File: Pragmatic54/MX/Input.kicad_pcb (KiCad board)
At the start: 2 copper layers, 126.5 x 103.6 mm, 109 parts, among them J1 Conn_02x04_Odd_Even, SW1 SW_Push_45deg, SW10 SW_Push_45deg, SW11 SW_Push_45deg, SW12 SW_Push_45deg, SW13 SW_Push_45deg, SW14 SW_Push_45deg, SW15 SW_Push_45deg, SW16 SW_Push_45deg, SW17 SW_Push_45deg, SW18 SW_Push_45deg, SW19 SW_Push_45deg, SW2 SW_Push_45deg, SW20 SW_Push_45deg, SW21 SW_Push_45deg, SW22 SW_Push_45deg, SW23 SW_Push_45deg, SW24 SW_Push_45deg, SW25 SW_Push_45deg, SW26 SW_Push_45deg, SW27 SW_Push_45deg, SW28 SW_Push_45deg, SW29 SW_Push_45deg, SW3 SW_Push_45deg, SW30 SW_Push_45deg, SW31 SW_Push_45deg, SW32 SW_Push_45deg, SW33 SW_Push_45deg, SW34 SW_Push_45deg, SW35 SW_Push_45deg, SW36 SW_Push_45deg, SW37 SW_Push_45deg, SW38 SW_Push_45deg, SW39 SW_Push_45deg, SW4 SW_Push_45deg, SW40 SW_Push_45deg, SW41 SW_Push_45deg, SW42 SW_Push_45deg, SW43 SW_Push_45deg, SW44 SW_Push_45deg, SW45 SW_Push_45deg, SW46 SW_Push_45deg, SW47 SW_Push_45deg, SW48 SW_Push_45deg, SW5 SW_Push_45deg, SW52 SW_Push_45deg, SW53 SW_Push_45deg, SW54 SW_Push_45deg, SW55 SW_Push_45deg, SW56 SW_Push_45deg, SW57 SW_Push_45deg, SW6 SW_Push_45deg, SW7 SW_Push_45deg, SW8 SW_Push_45deg, SW9 SW_Push_45deg

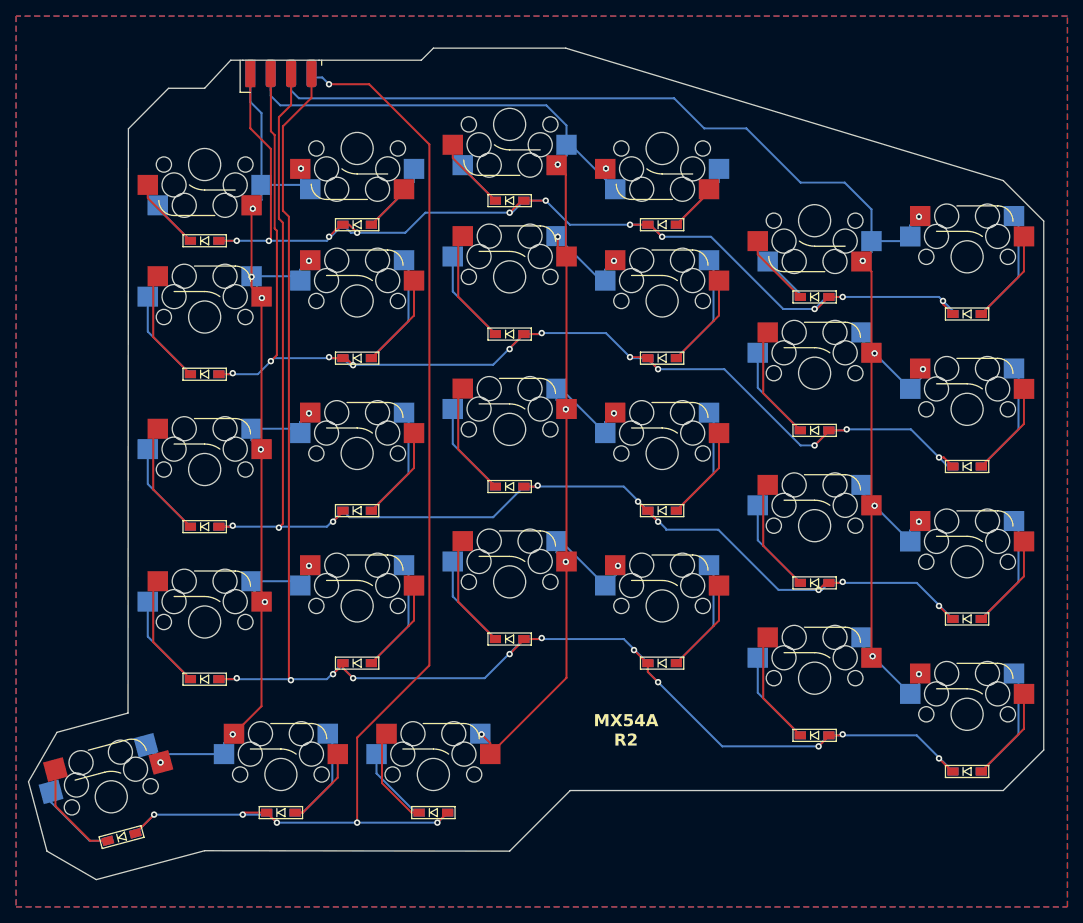
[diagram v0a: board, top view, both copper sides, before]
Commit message: MX54 R2.2 key switch on south
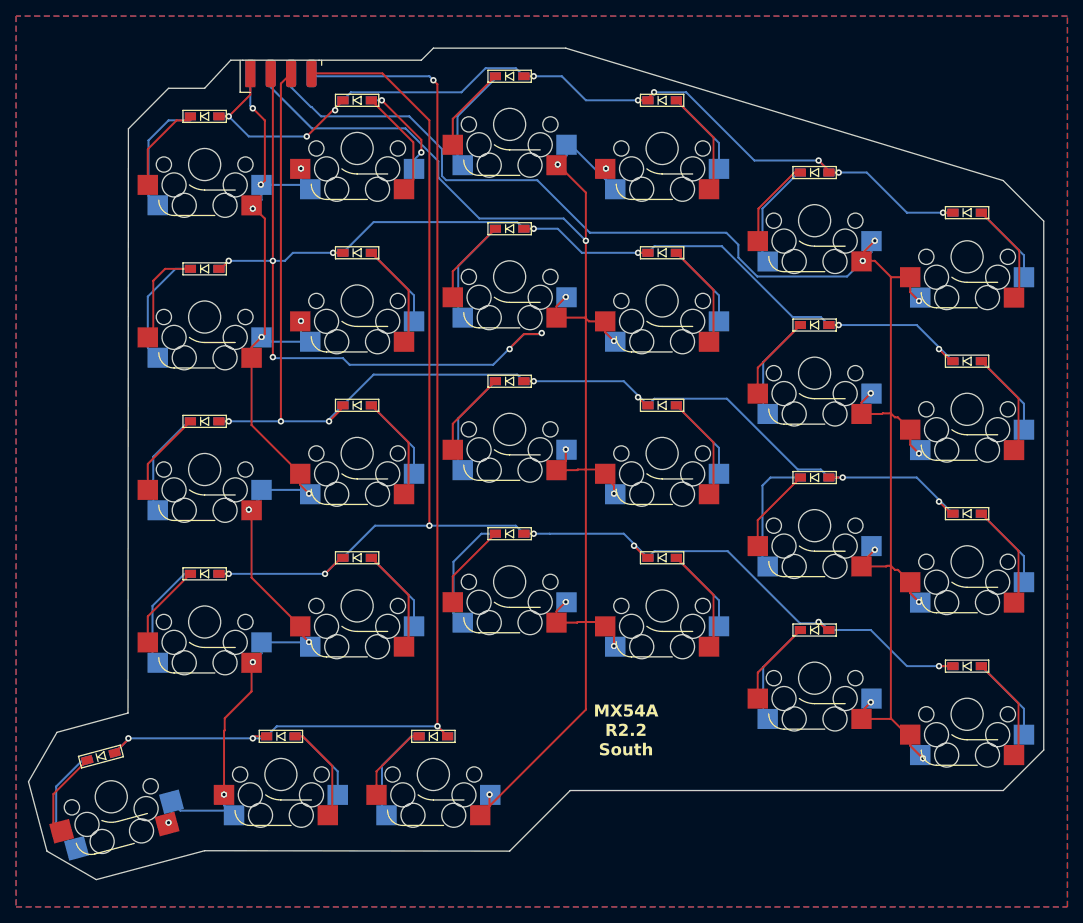
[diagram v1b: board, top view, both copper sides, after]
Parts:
- moved D10 15.5 mm to (104.5, 39.5)
- moved D11 15.5 mm to (123.5, 48.5)
- moved D2 15.5 mm to (123.5, 48.5)
- moved D3 15.5 mm to (104.5, 39.5)
- moved D4 15.5 mm to (85.5, 36.5)
- moved D5 15.5 mm to (66.5, 39.5)
- moved D6 15.5 mm to (47.5, 41.5)
- moved D7 15.5 mm to (47.5, 41.5)
- moved D8 15.5 mm to (66.5, 39.5)
- moved D9 15.5 mm to (85.5, 36.5)
- moved D13 13.1 mm to (142.5, 72.0)
- moved D14 13.1 mm to (123.5, 67.5)
- moved D15 13.1 mm to (104.5, 58.5)
- moved D16 13.1 mm to (85.5, 55.5)
- moved D17 13.1 mm to (66.5, 58.5)
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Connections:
- SW1 pad 1: C56 -> Net-(D1-A)
- SW1 pad 2: Net-(D1-A) -> C56
- SW12 pad 1: C56 -> Net-(D12-K)
- SW12 pad 2: Net-(D12-K) -> C56
- SW13 pad 1: C56 -> Net-(D13-A)
- SW13 pad 2: Net-(D13-A) -> C56
- SW14 pad 1: Net-(D14-K) -> C56
- SW14 pad 2: C56 -> Net-(D14-K)
- SW15 pad 1: C34 -> Net-(D15-A)
- SW15 pad 2: Net-(D15-A) -> C34
- SW16 pad 1: Net-(D16-K) -> C34
- SW16 pad 2: C34 -> Net-(D16-K)
- SW17 pad 1: C12 -> Net-(D17-A)
- SW17 pad 2: Net-(D17-A) -> C12
- SW18 pad 1: Net-(D18-K) -> C12
- SW18 pad 2: C12 -> Net-(D18-K)
- SW19 pad 1: Net-(D19-A) -> C12
- SW19 pad 2: C12 -> Net-(D19-A)
- SW20 pad 1: C12 -> Net-(D20-K)
- SW20 pad 2: Net-(D20-K) -> C12
- SW21 pad 1: Net-(D21-A) -> C34
- SW21 pad 2: C34 -> Net-(D21-A)
- SW22 pad 1: C34 -> Net-(D22-K)
- SW22 pad 2: Net-(D22-K) -> C34
- SW23 pad 1: Net-(D23-A) -> C56
- SW23 pad 2: C56 -> Net-(D23-A)
- SW24 pad 1: C56 -> Net-(D24-K)
- SW24 pad 2: Net-(D24-K) -> C56
- SW25 pad 1: C56 -> Net-(D25-A)
- SW25 pad 2: Net-(D25-A) -> C56
- SW26 pad 1: Net-(D26-K) -> C56
- SW26 pad 2: C56 -> Net-(D26-K)
- SW27 pad 1: C34 -> Net-(D27-A)
- SW27 pad 2: Net-(D27-A) -> C34
- SW28 pad 1: Net-(D28-K) -> C34
- SW28 pad 2: C34 -> Net-(D28-K)
- SW29 pad 1: C12 -> Net-(D29-A)
- SW29 pad 2: Net-(D29-A) -> C12
- SW30 pad 1: Net-(D30-K) -> C12
- SW30 pad 2: C12 -> Net-(D30-K)
- SW31 pad 1: Net-(D31-A) -> C12
- SW31 pad 2: C12 -> Net-(D31-A)
- SW32 pad 1: C12 -> Net-(D32-K)
- SW32 pad 2: Net-(D32-K) -> C12
- SW33 pad 1: Net-(D33-A) -> C34
- SW33 pad 2: C34 -> Net-(D33-A)
- SW34 pad 1: C34 -> Net-(D34-K)
- SW34 pad 2: Net-(D34-K) -> C34
- SW35 pad 1: Net-(D35-A) -> C56
- SW35 pad 2: C56 -> Net-(D35-A)
- SW36 pad 1: C56 -> Net-(D36-K)
- SW36 pad 2: Net-(D36-K) -> C56
- SW37 pad 1: C56 -> Net-(D37-A)
- SW37 pad 2: Net-(D37-A) -> C56
- SW38 pad 1: Net-(D38-K) -> C56
- SW38 pad 2: C56 -> Net-(D38-K)
- SW39 pad 1: C34 -> Net-(D39-A)
- SW39 pad 2: Net-(D39-A) -> C34
- SW40 pad 1: Net-(D40-K) -> C34
- SW40 pad 2: C34 -> Net-(D40-K)
- SW41 pad 1: C12 -> Net-(D41-A)
- SW41 pad 2: Net-(D41-A) -> C12
- SW42 pad 1: Net-(D42-K) -> C12
- SW42 pad 2: C12 -> Net-(D42-K)
- SW43 pad 1: Net-(D43-A) -> C12
- SW43 pad 2: C12 -> Net-(D43-A)
- SW44 pad 1: C12 -> Net-(D44-K)
- SW44 pad 2: Net-(D44-K) -> C12
- SW45 pad 1: Net-(D45-A) -> C34
- SW45 pad 2: C34 -> Net-(D45-A)
- SW46 pad 1: C34 -> Net-(D46-K)
- SW46 pad 2: Net-(D46-K) -> C34
- SW47 pad 1: Net-(D47-A) -> C56
- SW47 pad 2: C56 -> Net-(D47-A)
- SW48 pad 1: C56 -> Net-(D48-K)
- SW48 pad 2: Net-(D48-K) -> C56
- SW52 pad 1: Net-(D52-K) -> C34
- SW52 pad 2: C34 -> Net-(D52-K)
- SW53 pad 1: C12 -> Net-(D53-A)
- SW53 pad 2: Net-(D53-A) -> C12
- SW54 pad 1: Net-(D54-K) -> C12
- SW54 pad 2: C12 -> Net-(D54-K)
- SW55 pad 1: Net-(D55-A) -> C12
- SW55 pad 2: C12 -> Net-(D55-A)
- SW56 pad 1: C12 -> Net-(D56-K)
- SW56 pad 2: Net-(D56-K) -> C12
- SW57 pad 1: Net-(D57-A) -> C34
- SW57 pad 2: C34 -> Net-(D57-A)
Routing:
- net Row 2: track 160.7 -> 185.8 mm, vias 11 -> 10
- net Row 1: track 145.4 -> 121.2 mm, vias 11 -> 9
- net Row 4: track 204.3 -> 180.5 mm, vias 11 -> 7
- net Row 3: track 173.2 -> 156.2 mm, vias 9 -> 7
- net Row 5: track 157.7 -> 145.4 mm, vias 6 -> 4
- net C56: track 182.7 -> 194.3 mm, vias 8 -> 9
- net Net-(D7-A): track 6.10 -> 14.8 mm
- net C34: track 180.6 -> 188.4 mm, vias 9 -> 10
- net Net-(D5-A): track 6.10 -> 13.7 mm
- net Net-(D3-A): track 6.10 -> 12.4 mm
- net Net-(D11-A): track 6.10 -> 12.3 mm
- net Net-(D9-A): track 6.10 -> 12.1 mm
- net C12: track 145.8 -> 141.1 mm, vias 11 -> 12
- net Net-(D22-K): track 14.4 -> 10.7 mm
- net Net-(D20-K): track 14.4 -> 10.7 mm
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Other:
- board text added: "MX54A R2.2 South"
- board text removed: "MX54A R2"
